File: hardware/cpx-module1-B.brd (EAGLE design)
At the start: 80.6 x 106.3 mm, 72 parts, among them IC1 CIRCUITPLAYGROUNDEXPRESS, IC2 MCP6004, IC3 TL074, IC4 LM4040DIM3-5.0, J1 WQP-PJ301M-12_JACK, J2 WQP-PJ301M-12_JACK, J3 WQP-PJ301M-12_JACK, J4 WQP-PJ301M-12_JACK, J5 WQP-PJ301M-12_JACK, J6 WQP-PJ301M-12_JACK, J7 WQP-PJ301M-12_JACK, J8 WQP-PJ301M-12_JACK

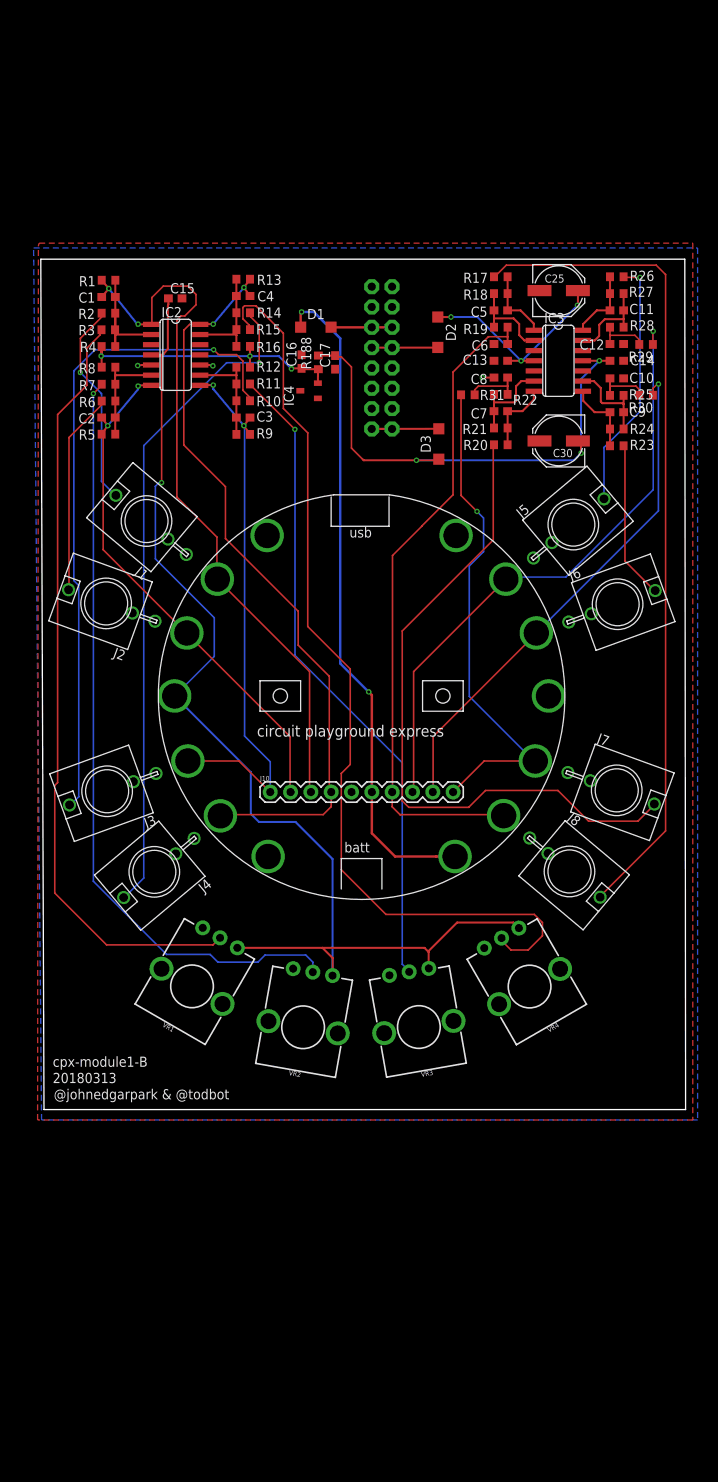
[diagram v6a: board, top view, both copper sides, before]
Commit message: fix silkscreen a little
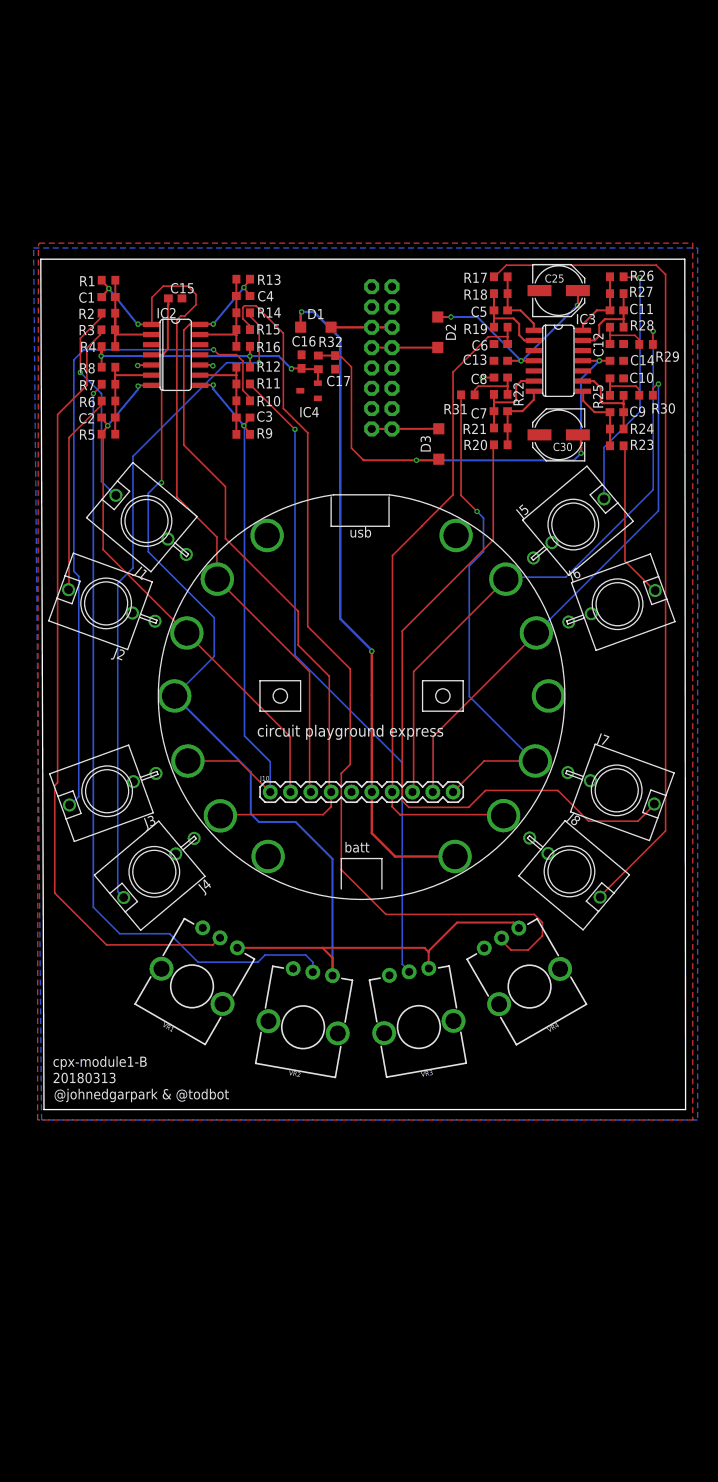
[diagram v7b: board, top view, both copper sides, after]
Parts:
- moved C30 0.76 mm to (24.6, 32.6)
- renumbered R188 to R32
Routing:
- net A5_KNOB: track 96.3 -> 98.2 mm
- net A6_JACK: track 83.2 -> 84.0 mm
- net +3V3: track 146.6 -> 147.4 mm
- net A7_JACK: track 83.0 -> 83.7 mm
